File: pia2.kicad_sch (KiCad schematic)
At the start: 34 parts, among them IC4 74ACT02, IC8 LM393DR, IC9 CD4050BDR, J2 6-bit DAC, U11 W65C21

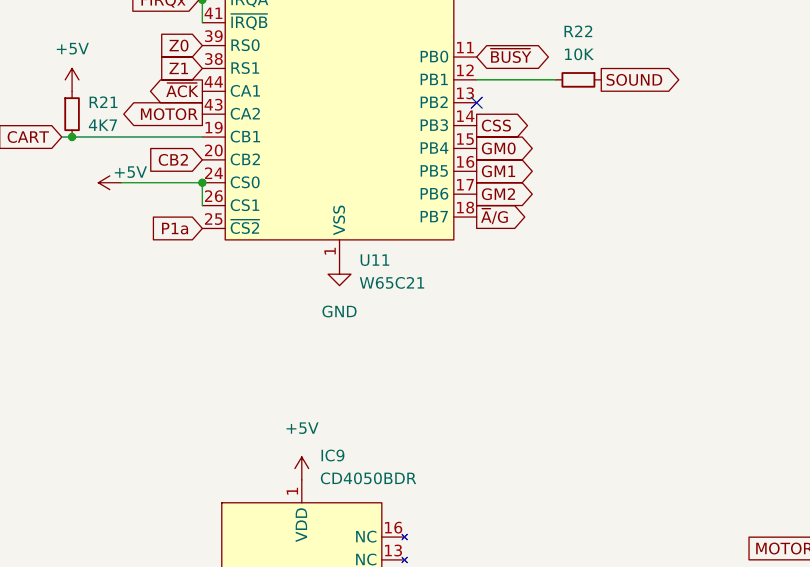
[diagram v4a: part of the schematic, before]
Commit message: add data bus to sam schematic
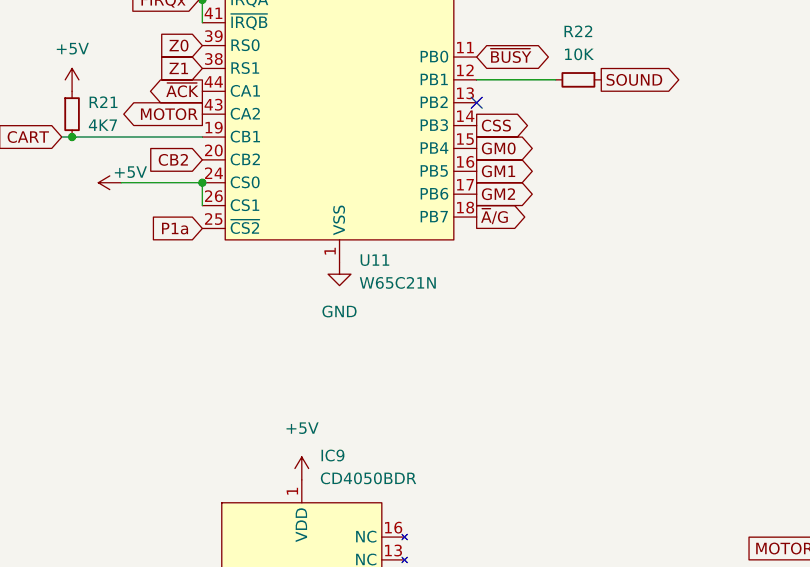
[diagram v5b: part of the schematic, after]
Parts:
- U11: value W65C21 -> W65C21N
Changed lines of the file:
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@@
 			)
 		)
-		(property "Value" "W65C21"
+		(property "Value" "W65C21N"
 			(at 67.3451 97.536 0)
 			(effects
@@
 			)
 		)
-		(property "Datasheet" ""
+		(property "Datasheet" "https://www.mouser.com/datasheet/2/436/w65c21-661.pdf"
 			(at 65.151 64.77 0)
 			(effects

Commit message: update vendor specific BOM fields
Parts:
- U11: DigiKey (none) -> ED90015-ND
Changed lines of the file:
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@@
+			)
+		)
+		(property "DigiKey" "ED90015-ND"
+			(at 65.151 64.77 0)
+			(effects
+				(font
+					(size 1.27 1.27)
+				)
+				(hide yes)
 			)
 		)

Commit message: add data bus transceiver
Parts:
- C27, C30: footprint Capacitor_SMD:CP_Elec_5x5.3 -> Capacitor_SMD:CP_Elec_4x5.4; DigiKey 732-8593-1-ND -> 732-8250-1-ND
- C28: DigiKey 399-13930-1-ND -> 399-C0805C220J5GAC7800CT-ND
- C29: DigiKey BC1074CT-ND -> 399-C0805C229D4HAC7800CT-ND
- C31: DigiKey BC2677CT-ND -> 399-15473-1-ND
- C32: DigiKey BC1101CT-ND -> 399-C0805C104K4RAC7800CT-ND
- R21, R23, R34: DigiKey CF14JT4K70CT-ND -> 541-4131-1-ND
- R22: DigiKey CF14JT10K0CT-ND -> RNCP0805FTD10K0CT-ND
- R24: DigiKey CF14JT68K0CT-ND -> 2019-RK73B2ATTD683JCT-ND
- R25: DigiKey CF14JT33K0CT-ND -> 2019-RK73B2ATTD333JCT-ND
- R26: DigiKey CF14JT1K00CT-ND -> RNCP0805FTD1K00CT-ND
- R27: DigiKey CF14JT1M50CT-ND -> 2019-RK73B2ATTD155JCT-ND
- R28, R30: DigiKey CF14JT56K0CT-ND -> 2019-RK73B2ATTD563JCT-ND
- R29: DigiKey CF14JT15K0CT-ND -> RNCP0805FTD15K0CT-ND
- R31: DigiKey CF14JT6K80CT-ND -> 2019-RK73B2ATTD682JCT-ND
- R32: DigiKey CF14JT8K20CT-ND -> 2019-RK73B2ATTD822JCT-ND
- R33: DigiKey CF14JT220RCT-ND -> 2019-RK73B2ATTD221JCT-ND
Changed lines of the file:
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@@
 			)
 		)
-		(property "DigiKey" "CF14JT10K0CT-ND"
+		(property "DigiKey" "RNCP0805FTD10K0CT-ND"
 			(at 91.694 74.93 0)
 			(effects
@@
 			)
 		)
-		(property "DigiKey" "BC1101CT-ND"
+		(property "DigiKey" "399-C0805C104K4RAC7800CT-ND"
 			(at 121.666 134.62 0)
 			(effects
@@
 			)
 		)
-		(property "DigiKey" "CF14JT8K20CT-ND"
+		(property "DigiKey" "2019-RK73B2ATTD822JCT-ND"
 			(at 208.661 47.498 0)
 			(effects
@@
 			)
 		)
-		(property "DigiKey" "CF14JT56K0CT-ND"
+		(property "DigiKey" "2019-RK73B2ATTD563JCT-ND"
 			(at 196.342 38.1 0)
 			(effects
@@
 			)
 		)
-		(property "DigiKey" "CF14JT1K00CT-ND"
+		(property "DigiKey" "RNCP0805FTD1K00CT-ND"
 			(at 171.704 28.829 0)
 			(effects
@@
 			)
 		)
-		(property "Footprint" "Capacitor_SMD:CP_Elec_5x5.3"
+		(property "Footprint" "Capacitor_SMD:CP_Elec_4x5.4"
 			(at 213.487 37.973 0)
 			(effects
@@
 			)
 		)
-		(property "DigiKey" "732-8593-1-ND"
+		(property "DigiKey" "732-8250-1-ND"
 			(at 213.487 37.973 0)
 			(effects
@@
 			)
 		)
-		(property "DigiKey" "CF14JT56K0CT-ND"
+		(property "DigiKey" "2019-RK73B2ATTD563JCT-ND"
 			(at 189.103 28.702 0)
 			(effects
@@
 			)
 		)
-		(property "DigiKey" "BC1074CT-ND"
+		(property "DigiKey" "399-C0805C229D4HAC7800CT-ND"
 			(at 145.161 75.438 0)
 			(effects
@@
 			)
 		)
-		(property "DigiKey" "CF14JT4K70CT-ND"
+		(property "DigiKey" "541-4131-1-ND"
 			(at 35.433 78.74 0)
 			(effects
@@
 			)
 		)
-		(property "DigiKey" "CF14JT33K0CT-ND"
+		(property "DigiKey" "2019-RK73B2ATTD333JCT-ND"
 			(at 157.353 75.438 0)
 			(effects
@@
 			)
 		)
-		(property "DigiKey" "CF14JT68K0CT-ND"
+		(property "DigiKey" "2019-RK73B2ATTD683JCT-ND"
 			(at 139.446 69.088 0)
 			(effects
@@
 			)
 		)
-		(property "DigiKey" "CF14JT4K70CT-ND"
+		(property "DigiKey" "541-4131-1-ND"
 			(at 179.07 148.59 0)
 			(effects
@@
 			)
 		)
-		(property "DigiKey" "CF14JT15K0CT-ND"
+		(property "DigiKey" "RNCP0805FTD15K0CT-ND"
 			(at 189.103 56.896 0)
 			(effects
@@
 			)
 		)
-		(property "Footprint" "Capacitor_SMD:CP_Elec_5x5.3"
+		(property "Footprint" "Capacitor_SMD:CP_Elec_4x5.4"
 			(at 59.69 26.924 0)
 			(effects
@@
 			)
 		)
-		(property "DigiKey" "732-8593-1-ND"
+		(property "DigiKey" "732-8250-1-ND"
 			(at 59.69 26.924 90)
 			(effects
@@
 			)
 		)
-		(property "DigiKey" "CF14JT1M50CT-ND"
+		(property "DigiKey" "2019-RK73B2ATTD155JCT-ND"
 			(at 179.959 32.639 0)
 			(effects
@@
 			)
 		)
-		(property "DigiKey" "CF14JT4K70CT-ND"
+		(property "DigiKey" "541-4131-1-ND"
 			(at 133.223 46.99 0)
 			(effects
@@
 			)
 		)
-		(property "DigiKey" "CF14JT220RCT-ND"
+		(property "DigiKey" "2019-RK73B2ATTD221JCT-ND"
 			(at 213.487 57.15 0)
 			(effects
@@
 			)
 		)
-		(property "DigiKey" "CF14JT6K80CT-ND"
+		(property "DigiKey" "2019-RK73B2ATTD682JCT-ND"
 			(at 199.771 47.498 0)
 			(effects
@@
 			)
 		)
-		(property "DigiKey" "BC2677CT-ND"
+		(property "DigiKey" "399-15473-1-ND"
 			(at 223.774 57.15 0)
 			(effects
@@
 			)
 		)
-		(property "DigiKey" "399-13930-1-ND"
+		(property "DigiKey" "399-C0805C220J5GAC7800CT-ND"
 			(at 136.398 75.438 0)
 			(effects
